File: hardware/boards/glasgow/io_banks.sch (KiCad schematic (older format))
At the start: 26 parts, among them J10 AUX, J4 Conn_01x02, J5 PinHeader_2x22_P1.27mm, U30 ICE40HX8K-BG121, U32 SN74LVC1T45DCKR

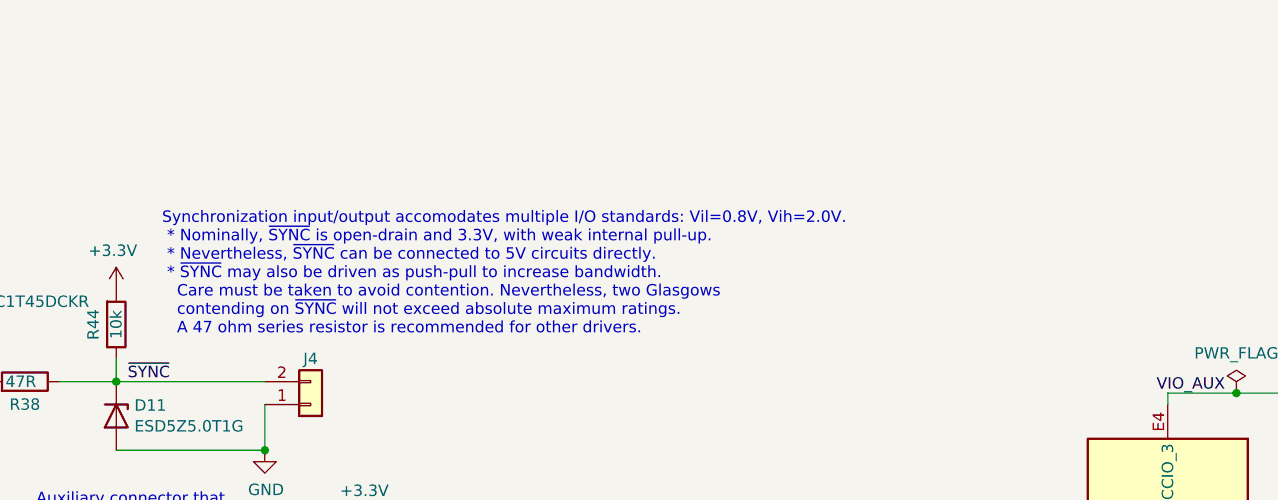
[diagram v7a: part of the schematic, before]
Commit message: fixed wrong spelled words
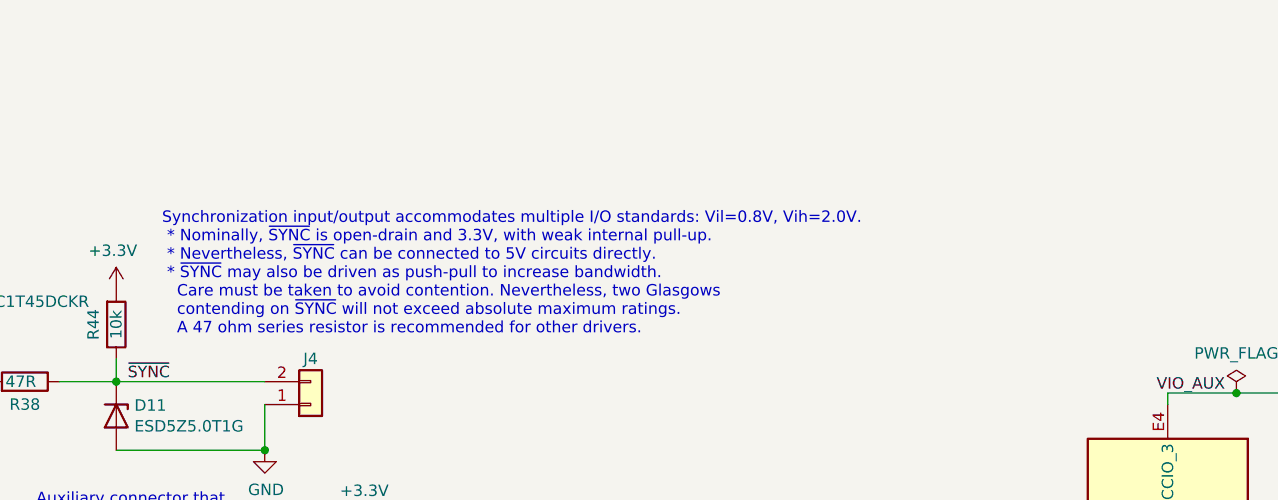
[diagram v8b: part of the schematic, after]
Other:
- note added: "Synchronization input/output accommodates multiple I/O standards: Vil=0.8V, Vih=2.0V.\n * Nominally, ~SYNC~ is open-drain and 3.3V, with weak internal pull-up.\n * Nevertheless, ~SYNC~ can be connected to 5V circuits directly.\n * ~SYNC~ may also be driven as push-pull to increase bandwidth.\n Care must be taken to avoid contention. Nevertheless, two Glasgows \n contending on ~SYNC~ will not exce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"
- note removed: "Synchronization input/output accomodates multiple I/O standards: Vil=0.8V, Vih=2.0V.\n * Nominally, ~SYNC~ is open-drain and 3.3V, with weak internal pull-up.\n * Nevertheless, ~SYNC~ can be connected to 5V circuits directly.\n * ~SYNC~ may also be driven as push-pull to increase bandwidth.\n Care must be taken to avoid contention. Nevertheless, two Glasgows \n contending on ~SYNC~ will not excee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"
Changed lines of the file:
@@
 	750  4950 900  4950
 Text Notes 3850 2200 0    50   ~ 0
-Synchronization input/output accomodates multiple I/O standards: Vil=0.8V, Vih=2.0V.\n * Nominally, ~SYNC~ is open-drain and 3.3V, with weak internal pull-up.\n * Nevertheless, ~SYNC~ can be connected to 5V circuits directly.\n * ~SYNC~ may also be driven as push-pull to increase bandwidth.\n   Care must be taken to avoid contention. Nevertheless, two Glasgows \n   contending on ~SYNC~ will not exceed absolute maximum ratings.\n   A 47 ohm series resistor is recommended for other drivers.
+Synchronization input/output accommodates multiple I/O standards: Vil=0.8V, Vih=2.0V.\n * Nominally, ~SYNC~ is open-drain and 3.3V, with weak internal pull-up.\n * Nevertheless, ~SYNC~ can be connected to 5V circuits directly.\n * ~SYNC~ may also be driven as push-pull to increase bandwidth.\n   Care must be taken to avoid contention. Nevertheless, two Glasgows \n   contending on ~SYNC~ will not exceed absolute maximum ratings.\n   A 47 ohm series resistor is recommended for other drivers.
 Wire Bus Line
 	5500 5800 6950 5800
